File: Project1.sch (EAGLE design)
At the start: 10 parts, among them IC1 MEGA8-AI

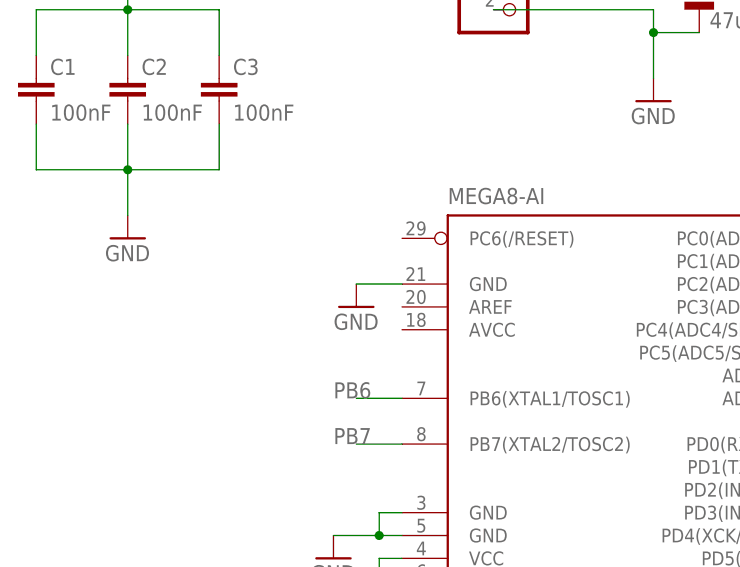
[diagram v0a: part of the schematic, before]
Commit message: modified shcamtic, add board
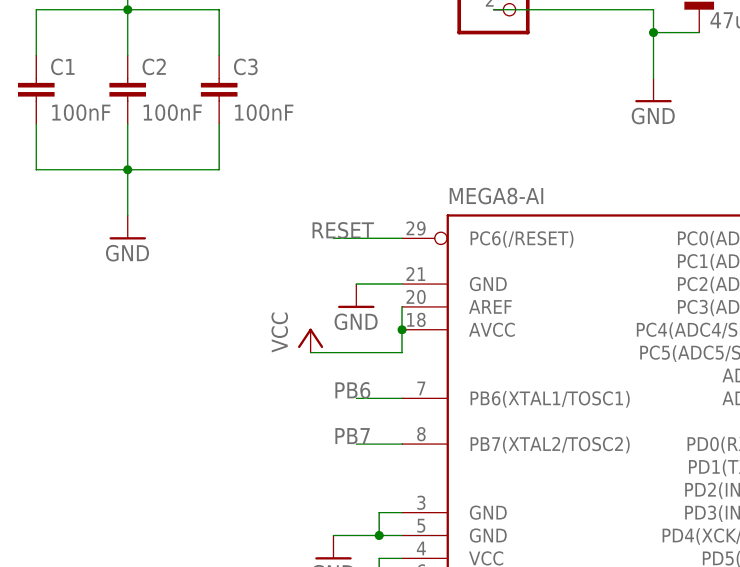
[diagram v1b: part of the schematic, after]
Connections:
- net RESET: now also IC1.PC6(/RESET)
- net VCC: now also IC1.AREF, IC1.AVCC
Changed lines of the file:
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@@
 <part name="P+7" library="supply1" library_urn="urn:adsk.eagle:library:371" deviceset="VCC" device=""/>
 <part name="C4" library="rcl" library_urn="urn:adsk.eagle:library:334" deviceset="CPOL-EU" device="E2.5-6" package3d_urn="urn:adsk.eagle:package:23349/1" value="47uF"/>
+<part name="P+8" library="supply1" library_urn="urn:adsk.eagle:library:371" deviceset="VCC" device=""/>
 </parts>
 <sheets>
@@
 <attribute name="VALUE" x="67.183" y="122.4026" size="1.778" layer="96"/>
 </instance>
+<instance part="P+8" gate="VCC" x="22.86" y="88.9" smashed="yes">
+<attribute name="VALUE" x="20.32" y="86.36" size="1.778" layer="96" rot="R90"/>
+</instance>
 </instances>
 <busses>
@@
 <wire x1="60.96" y1="15.24" x2="50.8" y2="15.24" width="0.1524" layer="91"/>
 <label x="45.72" y="15.24" size="1.778" layer="95"/>
+</segment>
+<segment>
+<pinref part="IC1" gate="G$1" pin="PC6(/RESET)"/>
+<wire x1="33.02" y1="99.06" x2="25.4" y2="99.06" width="0.1524" layer="91"/>
+<label x="22.86" y="99.06" size="1.778" layer="95"/>
 </segment>
 </net>
@@
 <junction x="60.96" y="129.54"/>
 </segment>
-</net>
+<segment>
+<pinref part="P+8" gate="VCC" pin="VCC"/>
+<pinref part="IC1" gate="G$1" pin="AVCC"/>
+<wire x1="22.86" y1="86.36" x2="33.02" y2="86.36" width="0.1524" layer="91"/>
+<wire x1="33.02" y1="86.36" x2="33.02" y2="88.9" width="0.1524" layer="91"/>
+<pinref part="IC1" gate="G$1" pin="AREF"/>
+<wire x1="33.02" y1="88.9" x2="33.02" y2="91.44" width="0.1524" layer="91"/>
+<junction x="33.02" y="88.9"/>
+</segment>
+</net>
